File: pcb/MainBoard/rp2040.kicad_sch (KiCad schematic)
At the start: 24 parts

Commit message: pcb progress
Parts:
- U401: renamed from U?; footprint RadPie2040:RP2040-QFN-56 -> led-matrix:RP2040-QFN-56
- gave numbers to parts that had none: 23
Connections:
- net XTAL_IN: now reaches C414.2, U401.20 (XTAL_IN), X401.3
- net XTAL_OUT: now reaches R404.2, U401.21 (XTAL_OUT)
- net XTAL_OUT_B: now reaches C415.2, R404.1, X401.1

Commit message: dump pcb
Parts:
- added C417: 22uF, Capacitor_SMD:C_1206_3216Metric, symbol Device:C
- C406: now not fitted; now left out of the parts list
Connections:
- net +3V3: now also C417.1
- net GND: now also C417.2
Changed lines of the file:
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@@
 		)
 	)
+	(wire
+		(pts
+			(xy 157.48 33.02) (xy 157.48 35.56)
+		)
+		(stroke
+			(width 0)
+			(type default)
+		)
+	)
 	(rectangle
 		(start 13.716 143.256)
@@
 	(rectangle
 		(start 13.462 13.462)
-		(end 144.78 142.24)
+		(end 186.69 142.24)
 		(stroke
 			(width 0.2)
@@
 		(unit 1)
 		(exclude_from_sim no)
-		(in_bom yes)
-		(on_board yes)
-		(dnp no)
+		(in_bom no)
+		(on_board no)
+		(dnp yes)
 		(property "Reference" "C406"
 			(at 68.58 22.8599 0)
@@
 	)
 	(symbol
+		(lib_id "power:GND")
+		(at 157.48 35.56 0)
+		(unit 1)
+		(exclude_from_sim no)
+		(in_bom yes)
+		(on_board yes)
+		(dnp no)
+		(fields_autoplaced yes)
+		(property "Reference" "#PWR0416"
+			(at 157.48 41.91 0)
+			(effects
+				(font
+					(size 1.27 1.27)
+				)
+				(hide yes)
+			)
+		)
+		(property "Value" "GND"
+			(at 157.48 40.64 0)
+			(effects
+				(font
+					(size 1.27 1.27)
+				)
+				(hide yes)
+			)
+		)
+		(property "Footprint" ""
+			(at 157.48 35.56 0)
+			(effects
+				(font
+					(size 1.27 1.27)
+				)
+				(hide yes)
+			)
+		)
+		(property "Datasheet" ""
+			(at 157.48 35.56 0)
+			(effects
+				(font
+					(size 1.27 1.27)
+				)
+				(hide yes)
+			)
+		)
+		(property "Description" "Power symbol creates a global label with name \"GND\" , ground"
+			(at 157.48 35.56 0)
+			(effects
+				(font
+					(size 1.27 1.27)
+				)
+				(hide yes)
+			)
+		)
+		(pin "1"
+		)
+		(instances
+			(project "MainBoard"
+				(path "/ac576ee3-ac6f-4244-babf-9af36c7a7db3/94f24be7-e4f5-4d4a-8789-064f4a08d889"
+					(reference "#PWR0416")
+					(unit 1)
+				)
+			)
+		)
+	)
+	(symbol
 		(lib_id "power:+3V3")
 		(at 43.18 43.18 0)
@@
 	)
 	(symbol
+		(lib_id "Device:C")
+		(at 157.48 29.21 0)
+		(unit 1)
+		(exclude_from_sim no)
+		(in_bom no)
+		(on_board no)
+		(dnp yes)
+		(fields_autoplaced yes)
+		(property "Reference" "C417"
+			(at 161.29 27.9399 0)
+			(effects
+				(font
+					(size 1.27 1.27)
+				)
+				(justify left)
+			)
+		)
+		(property "Value" "22uF"
+			(at 161.29 30.4799 0)
+			(effects
+				(font
+					(size 1.27 1.27)
+				)
+				(justify left)
+			)
+		)
+		(property "Footprint" "Capacitor_SMD:C_1206_3216Metric"
+			(at 158.4452 33.02 0)
+			(effects
+				(font
+					(size 1.27 1.27)
+				)
+				(hide yes)
+			)
+		)
+		(property "Datasheet" "~"
+			(at 157.48 29.21 0)
+			(effects
+				(font
+					(size 1.27 1.27)
+				)
+				(hide yes)
+			)
+		)
+		(property "Description" "Unpolarized capacitor"
+			(at 157.48 29.21 0)
+			(effects
+				(font
+					(size 1.27 1.27)
+				)
+				(hide yes)
+			)
+		)
+		(property "LCSC" "C12891"
+			(at 157.48 29.21 0)
+			(effects
+				(font
+					(size 1.27 1.27)
+				)
+				(hide yes)
+			)
+		)
+		(pin "2"
+		)
+		(pin "1"
+		)
+		(instances
+			(project "MainBoard"
+				(path "/ac576ee3-ac6f-4244-babf-9af36c7a7db3/94f24be7-e4f5-4d4a-8789-064f4a08d889"
+					(reference "C417")
+					(unit 1)
+				)
+			)
+		)
+	)
+	(symbol
 		(lib_id "Device:R")
 		(at 40.64 161.29 0)
@@
 					(unit 1)
 				)
+			)
+		)
+	)
+	(symbol
+		(lib_id "power:+3V3")
+		(at 157.48 25.4 0)
+		(unit 1)
+		(exclude_from_sim no)
+		(in_bom yes)
+		(on_board yes)
+		(dnp no)
+		(property "Reference" "#PWR0417"
+			(at 157.48 29.21 0)
+			(effects
+				(font
+					(size 1.27 1.27)
+				)
+				(hide yes)
+			)
+		)
+		(property "Value" "+3V3"
+			(at 153.924 22.352 0)
+			(effects
+				(font
+					(size 1.27 1.27)
+				)
+			)
+		)
+		(property "Footprint" ""
+			(at 157.48 25.4 0)
+			(effects
+				(font
+					(size 1.27 1.27)
+				)
+				(hide yes)
+			)
+		)
+		(property "Datasheet" ""
+			(at 157.48 25.4 0)
+			(effects
+				(font
+					(size 1.27 1.27)
+				)
+				(hide yes)
+			)
+		)
+		(property "Description" "Power symbol creates a global label with name \"+3V3\""
+			(at 157.48 25.4 0)
+			(effects
+				(font
+					(size 1.27 1.27)
+				)
+				(hide yes)
+			)
+		)
+		(pin "1"
+		)
+		(instances
+			(project "MainBoard"
+				(path "/ac576ee3-ac6f-4244-babf-9af36c7a7db3/94f24be7-e4f5-4d4a-8789-064f4a08d889"
+					(reference "#PWR0417")
+					(unit 1)
+				)

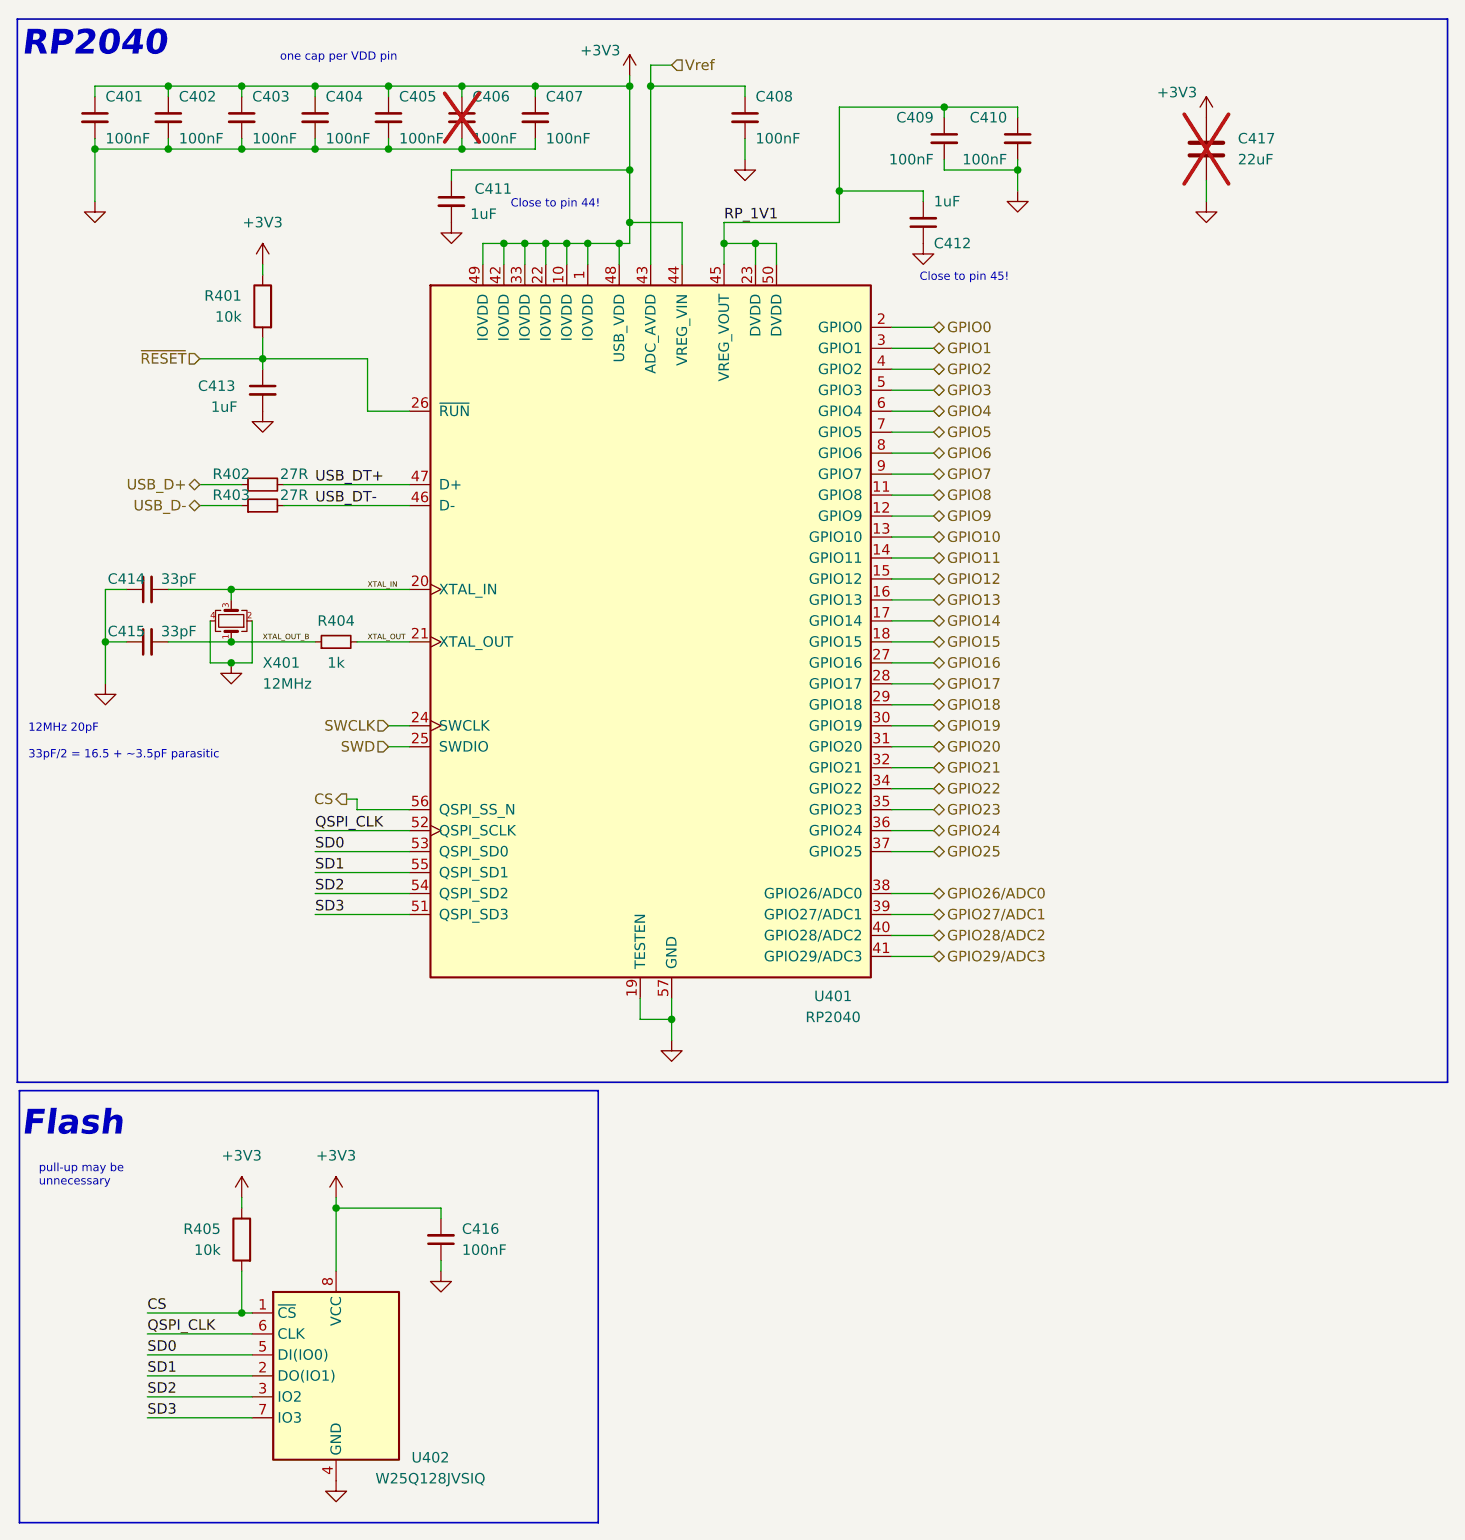
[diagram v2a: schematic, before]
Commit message: MainBoard: fixes, simplify, BOM optimize, DRC fixes, ERC fixes
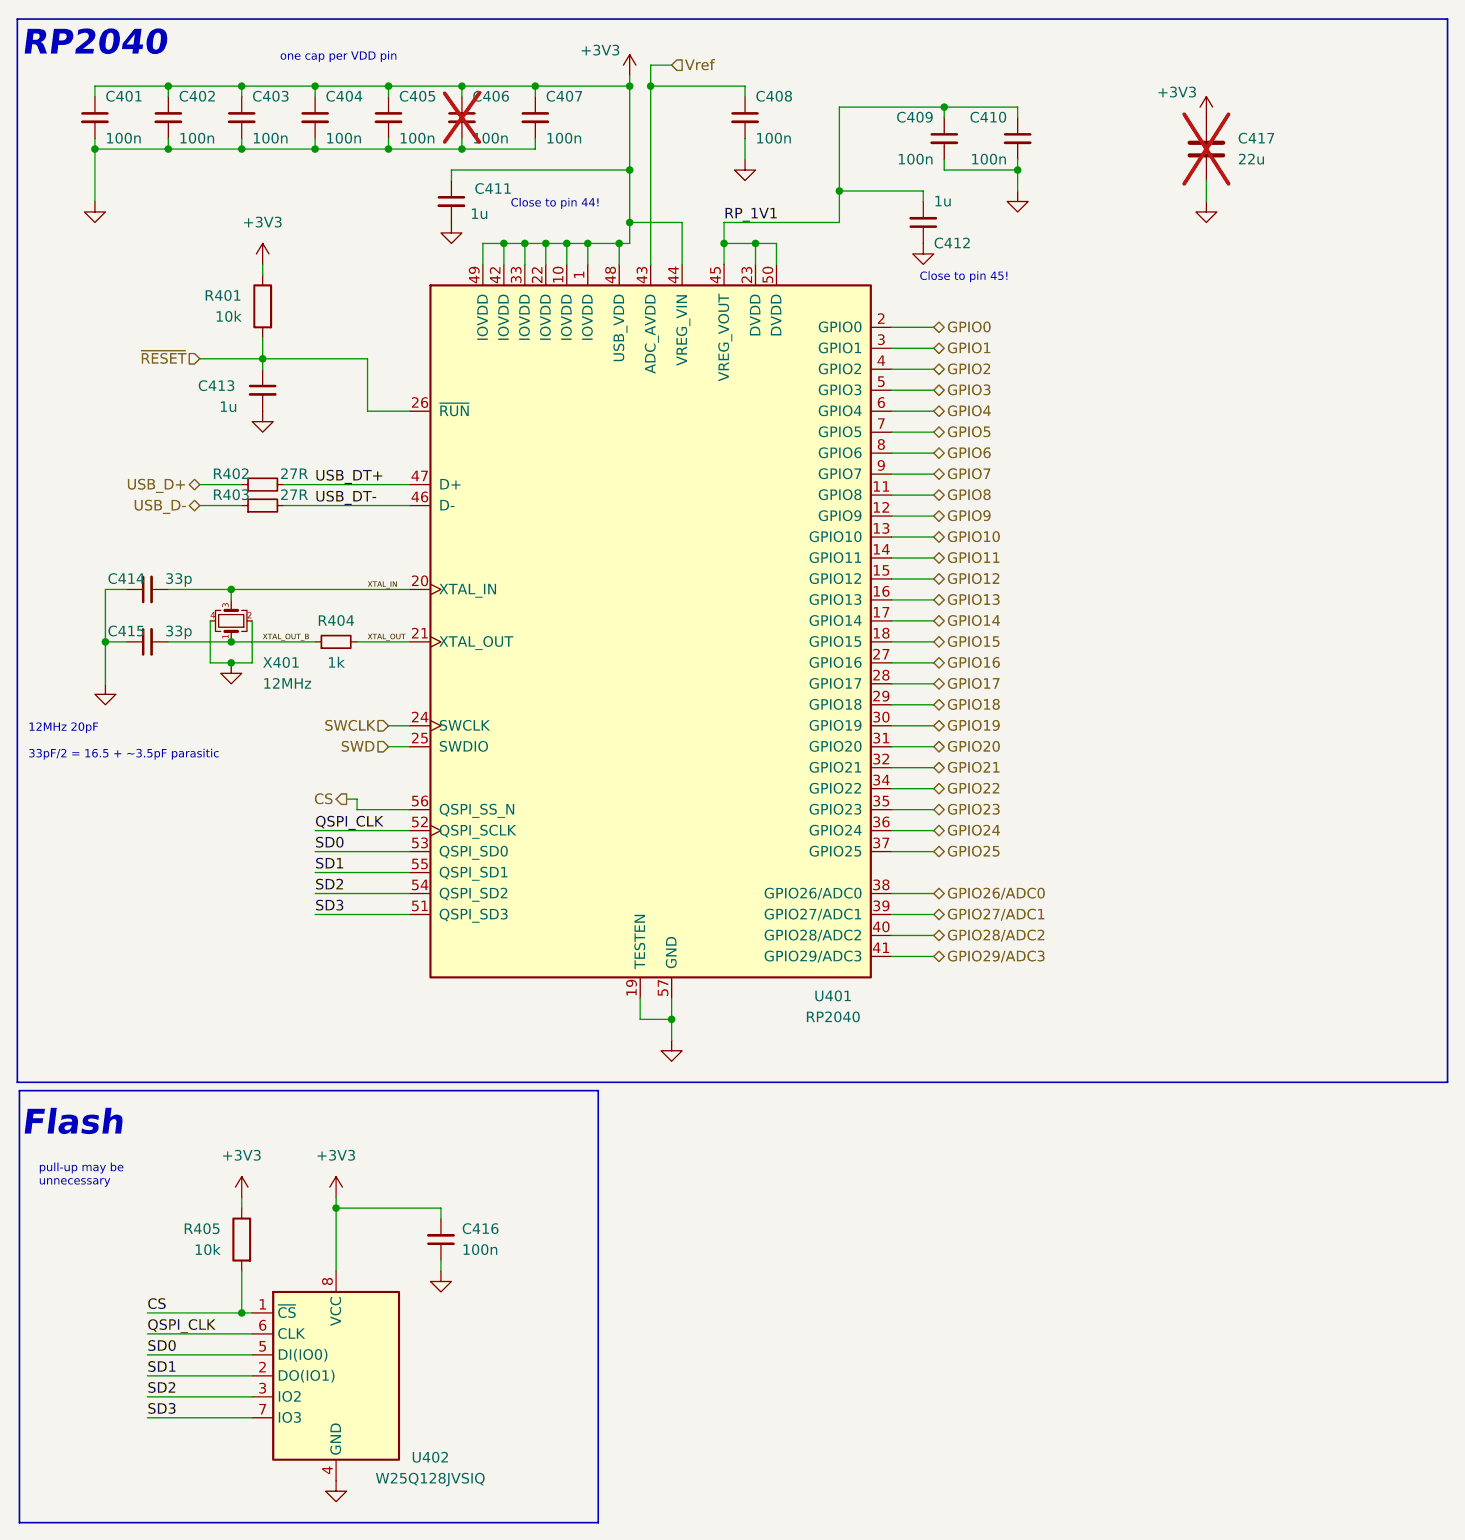
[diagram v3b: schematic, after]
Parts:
- C401, C402, C403, C404, C405, C406, C407, C408, C409, C410, C416: value 100nF -> 100n
- C411, C412, C413: value 1uF -> 1u
- C414, C415: value 33pF -> 33p
- C417: value 22uF -> 22u; footprint Capacitor_SMD:C_1206_3216Metric -> Capacitor_SMD:C_0805_2012Metric; LCSC C12891 -> C45783
- U401: now left out of the parts list
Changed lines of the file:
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@@
 	(wire
 		(pts
+			(xy 119.38 68.58) (xy 124.46 68.58)
+		)
+		(stroke
+			(width 0)
+			(type default)
+		)
+	)
+	(wire
+		(pts
 			(xy 86.36 40.64) (xy 87.63 40.64)
 		)
@@
 	(wire
 		(pts
-			(xy 119.38 68.58) (xy 124.46 68.58)
-		)
-		(stroke
-			(width 0)
-			(type default)
-		)
-	)
-	(wire
-		(pts
 			(xy 119.38 86.36) (xy 124.46 86.36)
 		)
@@
 			)
 		)
-		(property "Value" "100nF"
+		(property "Value" "100n"
 			(at 68.58 27.9399 0)
 			(effects
@@
 			)
 		)
-		(property "Value" "100nF"
+		(property "Value" "100n"
 			(at 41.91 27.9399 0)
 			(effects
@@
 			)
 		)
-		(property "Value" "100nF"
+		(property "Value" "100n"
 			(at 67.31 162.5535 0)
 			(effects
@@
 			)
 		)
-		(property "Value" "22uF"
+		(property "Value" "22u"
 			(at 161.29 30.4799 0)
 			(effects
@@
 			)
 		)
-		(property "Footprint" "Capacitor_SMD:C_1206_3216Metric"
+		(property "Footprint" "Capacitor_SMD:C_0805_2012Metric"
 			(at 158.4452 33.02 0)
 			(effects
@@
 			)
 		)
-		(property "LCSC" "C12891"
+		(property "LCSC" "C45783"
 			(at 157.48 29.21 0)
 			(effects
@@
 			)
 		)
-		(property "Value" "33pF"
+		(property "Value" "33p"
 			(at 33.02 81.28 90)
 			(effects
@@
 			)
 		)
-		(property "Value" "1uF"
+		(property "Value" "1u"
 			(at 68.326 37.084 0)
 			(effects
@@
 			)
 		)
-		(property "Value" "100nF"
+		(property "Value" "100n"
 			(at 50.8 27.9399 0)
 			(effects
@@
 			)
 		)
-		(property "Value" "100nF"
+		(property "Value" "100n"
 			(at 59.69 27.9399 0)
 			(effects
@@
 		(unit 1)
 		(exclude_from_sim no)
-		(in_bom yes)
+		(in_bom no)
 		(on_board yes)
 		(dnp no)
@@
 			)
 		)
-		(property "Value" "1uF"
+		(property "Value" "1u"
 			(at 40.132 60.452 0)
 			(effects
@@
 			)
 		)
-		(property "Value" "33pF"
+		(property "Value" "33p"
 			(at 33.02 87.63 90)
 			(effects
@@
 			)
 		)
-		(property "Value" "1uF"
+		(property "Value" "1u"
 			(at 124.46 35.5601 0)
 			(effects
@@
 			)
 		)
-		(property "Value" "100nF"
+		(property "Value" "100n"
 			(at 133.35 30.4799 0)
 			(effects
@@
 			)
 		)
-		(property "Value" "100nF"
+		(property "Value" "100n"
 			(at 33.02 27.9399 0)
 			(effects
@@
 			)
 		)
-		(property "Value" "100nF"
+		(property "Value" "100n"
 			(at 24.13 27.9399 0)
 			(effects
@@
 			)
 		)
-		(property "Value" "100nF"
+		(property "Value" "100n"
 			(at 77.47 27.9399 0)
 			(effects
@@
 			)
 		)
-		(property "Value" "100nF"
+		(property "Value" "100n"
 			(at 102.87 27.9399 0)
 			(effects
@@
 			)
 		)
-		(property "Value" "100nF"
+		(property "Value" "100n"
 			(at 124.46 30.4799 0)
 			(effects

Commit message: pcb: fixes, improvements
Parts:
- added C418: 22u, Capacitor_SMD:C_0805_2012Metric, symbol Device:C
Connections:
- net +3V3: now also C418.1
- net GND: now also C418.2
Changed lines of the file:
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@@
 	)
 	(junction
+		(at 64.77 157.48)
+		(diameter 0)
+		(color 0 0 0 0)
+	)
+	(junction
 		(at 87.63 31.75)
 		(diameter 0)
@@
 	)
 	(junction
+		(at 64.77 165.1)
+		(diameter 0)
+		(color 0 0 0 0)
+	)
+	(junction
 		(at 24.13 88.9)
 		(diameter 0)
@@
 	(wire
 		(pts
+			(xy 76.2 165.1) (xy 64.77 165.1)
+		)
+		(stroke
+			(width 0)
+			(type default)
+		)
+	)
+	(wire
+		(pts
 			(xy 22.86 21.59) (xy 31.75 21.59)
 		)
@@
 	(wire
 		(pts
+			(xy 64.77 166.37) (xy 64.77 165.1)
+		)
+		(stroke
+			(width 0)
+			(type default)
+		)
+	)
+	(wire
+		(pts
 			(xy 102.87 40.64) (xy 102.87 43.18)
 		)
@@
 	(wire
 		(pts
+			(xy 64.77 157.48) (xy 76.2 157.48)
+		)
+		(stroke
+			(width 0)
+			(type default)
+		)
+	)
+	(wire
+		(pts
 			(xy 88.9 132.08) (xy 88.9 134.62)
 		)
@@
 	(rectangle
 		(start 13.716 143.256)
-		(end 83.82 195.58)
+		(end 96.52 195.58)
 		(stroke
 			(width 0.2)
@@
 	(symbol
 		(lib_id "power:GND")
-		(at 64.77 165.1 0)
+		(at 64.77 166.37 0)
 		(unit 1)
 		(exclude_from_sim no)
@@
 		(dnp no)
 		(property "Reference" "#PWR0414"
-			(at 64.77 171.45 0)
+			(at 64.77 172.72 0)
 			(effects
 				(font
@@
 		)
 		(property "Value" "GND"
-			(at 69.85 165.1 0)
+			(at 69.85 166.37 0)
 			(effects
 				(font
@@
 		)
 		(property "Footprint" ""
-			(at 64.77 165.1 0)
+			(at 64.77 166.37 0)
 			(effects
 				(font
@@
 		)
 		(property "Datasheet" ""
-			(at 64.77 165.1 0)
+			(at 64.77 166.37 0)
 			(effects
 				(font
@@
 		)
 		(property "Description" "Power symbol creates a global label with name \"GND\" , ground"
-			(at 64.77 165.1 0)
+			(at 64.77 166.37 0)
 			(effects
 				(font
@@
 					(unit 1)
 				)
+			)
+		)
+	)
+	(symbol
+		(lib_id "Device:C")
+		(at 76.2 161.29 0)
+		(unit 1)
+		(exclude_from_sim no)
+		(in_bom yes)
+		(on_board yes)
+		(dnp no)
+		(property "Reference" "C418"
+			(at 80.01 160.0199 0)
+			(effects
+				(font
+					(size 1.27 1.27)
+				)
+				(justify left)
+			)
+		)
+		(property "Value" "22u"
+			(at 80.01 162.5599 0)
+			(effects
+				(font
+					(size 1.27 1.27)
+				)
+				(justify left)
+			)
+		)
+		(property "Footprint" "Capacitor_SMD:C_0805_2012Metric"
+			(at 77.1652 165.1 0)
+			(effects
+				(font
+					(size 1.27 1.27)
+				)
+				(hide yes)
+			)
+		)
+		(property "Datasheet" "~"
+			(at 76.2 161.29 0)
+			(effects
+				(font
+					(size 1.27 1.27)
+				)
+				(hide yes)
+			)
+		)
+		(property "Description" "Unpolarized capacitor"
+			(at 76.2 161.29 0)
+			(effects
+				(font
+					(size 1.27 1.27)
+				)
+				(hide yes)
+			)
+		)
+		(property "LCSC" "C45783"
+			(at 76.2 161.29 0)
+			(effects
+				(font
+					(size 1.27 1.27)
+				)
+				(hide yes)
+			)
+		)
+		(pin "2"
+		)
+		(pin "1"
+		)
+		(instances
+			(project "MainBoard"
+				(path "/ac576ee3-ac6f-4244-babf-9af36c7a7db3/94f24be7-e4f5-4d4a-8789-064f4a08d889"
+					(reference "C418")
+					(unit 1)
+				)
